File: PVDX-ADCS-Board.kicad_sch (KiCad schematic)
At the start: 0 parts

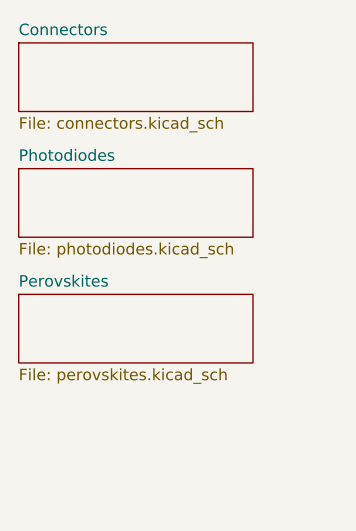
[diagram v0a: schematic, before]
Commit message: Add h-bridges for magnetorquers
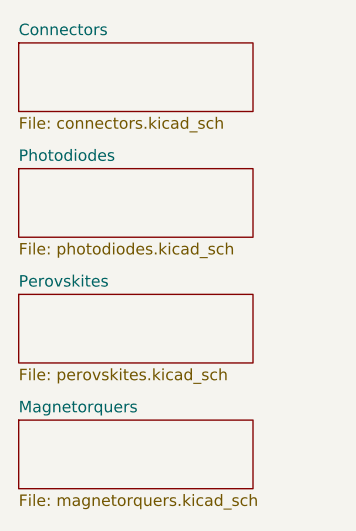
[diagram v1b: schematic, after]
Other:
- added sheet Magnetorquers (magnetorquers.kicad_sch)
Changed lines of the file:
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@@
+	)
+	(sheet
+		(at 64.77 140.97)
+		(size 26.035 7.62)
+		(exclude_from_sim no)
+		(in_bom yes)
+		(on_board yes)
+		(dnp no)
+		(fields_autoplaced yes)
+		(stroke
+			(width 0.1524)
+			(type solid)
+		)
+		(fill
+			(color 0 0 0 0)
+		)
+		(property "Sheetname" "Magnetorquers"
+			(at 64.77 140.2584 0)
+			(show_name no)
+			(do_not_autoplace no)
+			(effects
+				(font
+					(size 1.27 1.27)
+				)
+				(justify left bottom)
+			)
+		)
+		(property "Sheetfile" "magnetorquers.kicad_sch"
+			(at 64.77 149.1746 0)
+			(show_name no)
+			(do_not_autoplace no)
+			(effects
+				(font
+					(size 1.27 1.27)
+				)
+				(justify left top)
+			)
+		)
+		(instances
+			(project "PVDX-ADCS-Board"
+				(path "/fbb597ca-297a-4338-ae0d-7994cc902267"
+					(page "5")
+				)
+			)
+		)
 	)
 	(sheet
